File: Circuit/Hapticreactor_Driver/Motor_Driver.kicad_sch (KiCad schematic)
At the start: 5 parts, among them J1 Conn_01x02, J2 Conn_01x02, U2 TB6552FNG_C_8_EL

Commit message: ハプティックリアクタ用基板完成
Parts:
- removed C2: 0.1u, Capacitor_SMD:C_0603_1608Metric_Pad1.08x0.95mm_HandSolder, symbol Device:C
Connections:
- net +5V is gone; now on net +3.3V: U2.6 (VM)
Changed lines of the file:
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@@
 	(paper "A4")
-	(junction
-		(at 199.39 80.01)
-		(diameter 0)
-		(color 0 0 0 0)
-	)
 	(junction
 		(at 172.72 83.82)
@@
 	(wire
 		(pts
-			(xy 199.39 80.01) (xy 207.01 80.01)
-		)
-		(stroke
-			(width 0)
-			(type default)
-		)
-	)
-	(wire
-		(pts
-			(xy 199.39 80.01) (xy 199.39 82.55)
-		)
-		(stroke
-			(width 0)
-			(type default)
-		)
-	)
-	(wire
-		(pts
-			(xy 207.01 76.2) (xy 207.01 80.01)
+			(xy 199.39 76.2) (xy 199.39 82.55)
 		)
 		(stroke
@@
 		(pts
 			(xy 176.53 96.52) (xy 176.53 91.44)
-		)
-		(stroke
-			(width 0)
-			(type default)
-		)
-	)
-	(wire
-		(pts
-			(xy 199.39 76.2) (xy 199.39 80.01)
 		)
 		(stroke
@@
 	)
 	(symbol
-		(lib_id "power:+3.3V")
-		(at 207.01 68.58 0)
-		(unit 1)
-		(exclude_from_sim no)
-		(in_bom yes)
-		(on_board yes)
-		(dnp no)
-		(fields_autoplaced yes)
-		(property "Reference" "#PWR06"
-			(at 207.01 72.39 0)
-			(effects
-				(font
-					(size 1.27 1.27)
-				)
-				(hide yes)
-			)
-		)
-		(property "Value" "+3.3V"
-			(at 207.01 63.5 0)
-			(effects
-				(font
-					(size 1.27 1.27)
-				)
-			)
-		)
-		(property "Footprint" ""
-			(at 207.01 68.58 0)
-			(effects
-				(font
-					(size 1.27 1.27)
-				)
-				(hide yes)
-			)
-		)
-		(property "Datasheet" ""
-			(at 207.01 68.58 0)
-			(effects
-				(font
-					(size 1.27 1.27)
-				)
-				(hide yes)
-			)
-		)
-		(property "Description" "Power symbol creates a global label with name \"+3.3V\""
-			(at 207.01 68.58 0)
-			(effects
-				(font
-					(size 1.27 1.27)
-				)
-				(hide yes)
-			)
-		)
-		(pin "1"
-		)
-		(instances
-			(project "Hapticreactor_Driver"
-				(path "/2de60640-83cc-436b-97a4-426b15b610d6/dde69832-1fdb-4162-bbfc-013df7eb0793"
-					(reference "#PWR06")
-					(unit 1)
-				)
-			)
-		)
-	)
-	(symbol
 		(lib_id "Connector_Generic:Conn_01x02")
 		(at 233.68 80.01 0)
@@
 				(path "/2de60640-83cc-436b-97a4-426b15b610d6/dde69832-1fdb-4162-bbfc-013df7eb0793"
 					(reference "J1")
+					(unit 1)
+				)
+			)
+		)
+	)
+	(symbol
+		(lib_id "power:+3.3V")
+		(at 121.92 69.85 0)
+		(unit 1)
+		(exclude_from_sim no)
+		(in_bom yes)
+		(on_board yes)
+		(dnp no)
+		(fields_autoplaced yes)
+		(property "Reference" "#PWR04"
+			(at 121.92 73.66 0)
+			(effects
+				(font
+					(size 1.27 1.27)
+				)
+				(hide yes)
+			)
+		)
+		(property "Value" "+3.3V"
+			(at 121.92 64.77 0)
+			(effects
+				(font
+					(size 1.27 1.27)
+				)
+			)
+		)
+		(property "Footprint" ""
+			(at 121.92 69.85 0)
+			(effects
+				(font
+					(size 1.27 1.27)
+				)
+				(hide yes)
+			)
+		)
+		(property "Datasheet" ""
+			(at 121.92 69.85 0)
+			(effects
+				(font
+					(size 1.27 1.27)
+				)
+				(hide yes)
+			)
+		)
+		(property "Description" "Power symbol creates a global label with name \"+3.3V\""
+			(at 121.92 69.85 0)
+			(effects
+				(font
+					(size 1.27 1.27)
+				)
+				(hide yes)
+			)
+		)
+		(pin "1"
+		)
+		(instances
+			(project ""
+				(path "/2de60640-83cc-436b-97a4-426b15b610d6/dde69832-1fdb-4162-bbfc-013df7eb0793"
+					(reference "#PWR04")
 					(unit 1)
 				)
@@
 	)
 	(symbol
-		(lib_id "Device:C")
-		(at 207.01 72.39 0)
-		(unit 1)
-		(exclude_from_sim no)
-		(in_bom yes)
-		(on_board yes)
-		(dnp no)
-		(fields_autoplaced yes)
-		(property "Reference" "C2"
-			(at 210.82 71.1199 0)
-			(effects
-				(font
-					(size 1.27 1.27)
-				)
-				(justify left)
-			)
-		)
-		(property "Value" "0.1u"
-			(at 210.82 73.6599 0)
-			(effects
-				(font
-					(size 1.27 1.27)
-				)
-				(justify left)
-			)
-		)
-		(property "Footprint" "Capacitor_SMD:C_0603_1608Metric_Pad1.08x0.95mm_HandSolder"
-			(at 207.9752 76.2 0)
-			(effects
-				(font
-					(size 1.27 1.27)
-				)
-				(hide yes)
-			)
-		)
-		(property "Datasheet" "~"
-			(at 207.01 72.39 0)
-			(effects
-				(font
-					(size 1.27 1.27)
-				)
-				(hide yes)
-			)
-		)
-		(property "Description" "Unpolarized capacitor"
-			(at 207.01 72.39 0)
-			(effects
-				(font
-					(size 1.27 1.27)
-				)
-				(hide yes)
-			)
-		)
-		(pin "1"
-		)
-		(pin "2"
-		)
-		(instances
-			(project "Hapticreactor_Driver"
-				(path "/2de60640-83cc-436b-97a4-426b15b610d6/dde69832-1fdb-4162-bbfc-013df7eb0793"
-					(reference "C2")
-					(unit 1)
-				)
-			)
-		)
-	)
-	(symbol
 		(lib_id "TB6552FNG:TB6552FNG_C_8_EL")
 		(at 127 73.66 0)
@@
 					(unit 1)
 				)
-			)
-		)
-	)
-	(symbol
-		(lib_id "power:+5V")
-		(at 121.92 69.85 0)
-		(unit 1)
-		(exclude_from_sim no)
-		(in_bom yes)
-		(on_board yes)
-		(dnp no)
-		(fields_autoplaced yes)
-		(property "Reference" "#PWR04"
-			(at 121.92 73.66 0)
-			(effects
-				(font
-					(size 1.27 1.27)
-				)
-				(hide yes)
-			)
-		)
-		(property "Value" "+5V"
-			(at 121.92 64.77 0)
-			(effects
-				(font
-					(size 1.27 1.27)
-				)
-			)
-		)
-		(property "Footprint" ""
-			(at 121.92 69.85 0)
-			(effects
-				(font
-					(size 1.27 1.27)
-				)
-				(hide yes)
-			)
-		)
-		(property "Datasheet" ""
-			(at 121.92 69.85 0)
-			(effects
-				(font
-					(size 1.27 1.27)
-				)
-				(hide yes)
-			)
-		)
-		(property "Description" "Power symbol creates a global label with name \"+5V\""
-			(at 121.92 69.85 0)
-			(effects
-				(font
-					(size 1.27 1.27)
-				)
-				(hide yes)
-			)
-		)
-		(pin "1"
-		)
-		(instances
-			(project ""
-				(path "/2de60640-83cc-436b-97a4-426b15b610d6/dde69832-1fdb-4162-bbfc-013df7eb0793"
-					(reference "#PWR04")
-					(unit 1)
-				)

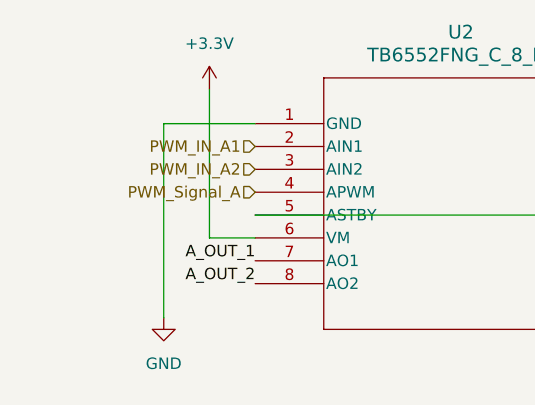
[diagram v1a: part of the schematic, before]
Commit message: VMをバッテリ入力に変更，バッテリ周りの間違いを訂正
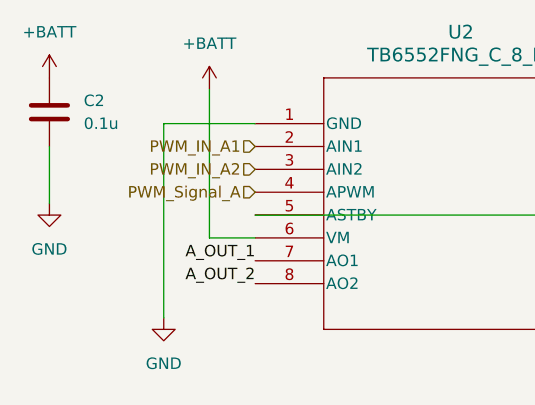
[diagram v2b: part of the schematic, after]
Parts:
- added C2: 0.1u, Capacitor_SMD:C_0603_1608Metric_Pad1.08x0.95mm_HandSolder, symbol Device:C
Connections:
- net +3.3V: no longer U2.6 (VM)
- net GND: now also C2.2
- new net +BATT: C2.1, U2.6 (VM)

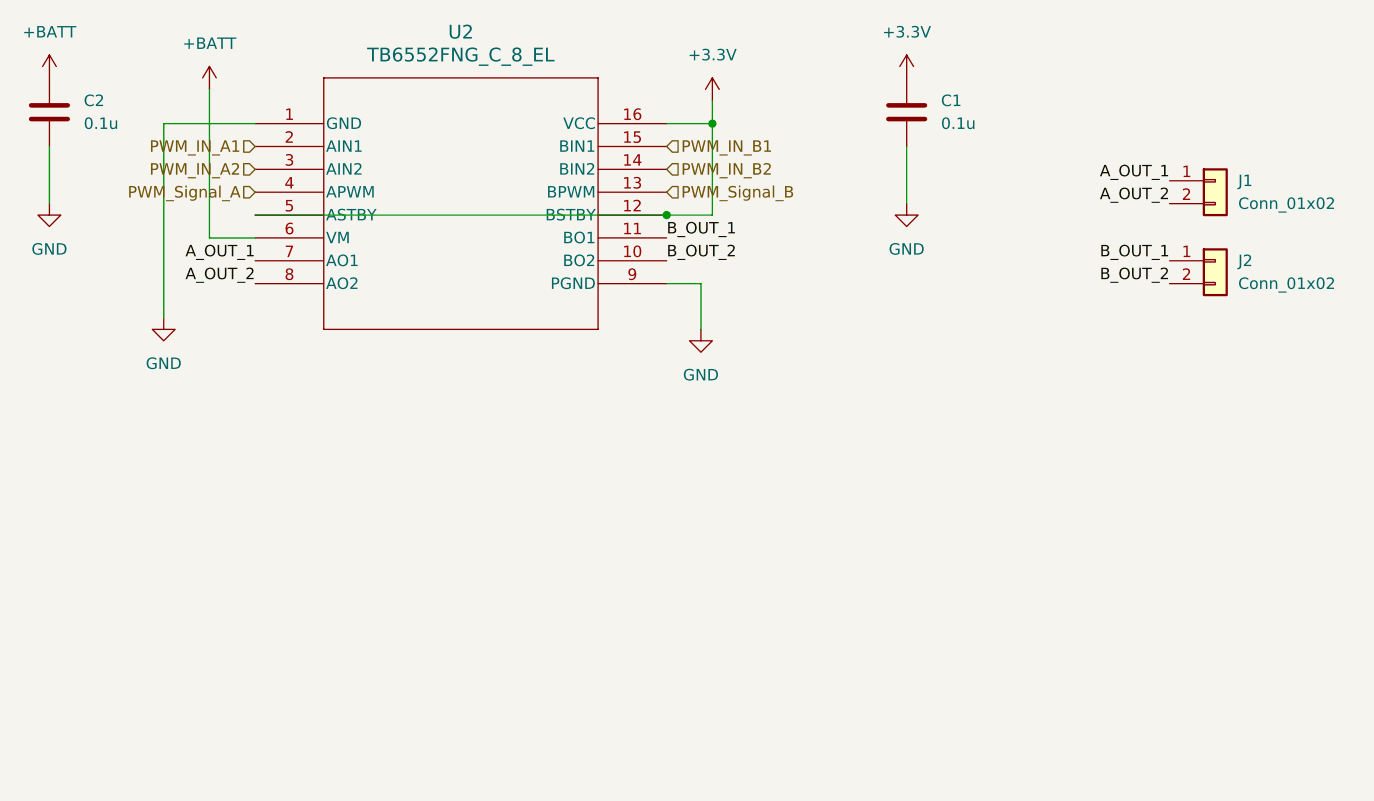
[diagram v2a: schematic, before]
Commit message: 秋野の回路に昇圧DCDCつけて東芝MDつけた
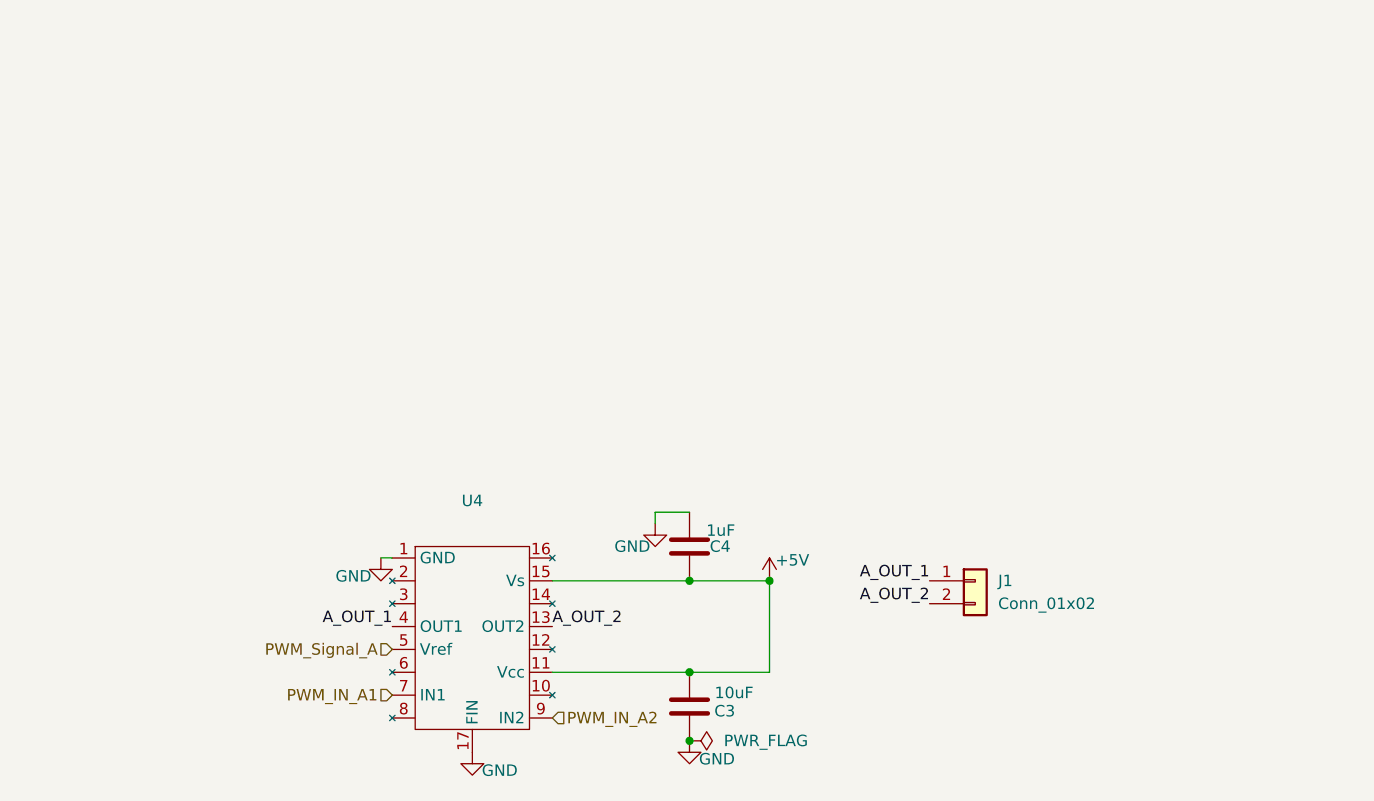
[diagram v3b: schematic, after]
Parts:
- removed C1, C2: 0.1u, Capacitor_SMD:C_0603_1608Metric_Pad1.08x0.95mm_HandSolder, symbol Device:C
- removed J2: Conn_01x02, Connector_PinHeader_2.00mm:PinHeader_1x02_P2.00mm_Vertical, symbol Connector_Generic:Conn_01x02
- removed U2: TB6552FNG_C_8_EL, User:TB6552FNG, symbol TB6552FNG:TB6552FNG_C_8_EL
- added C3: 10uF, Capacitor_SMD:C_0603_1608Metric, symbol Device:C
- added C4: 1uF, Capacitor_SMD:C_0603_1608Metric, symbol Device:C
- added U4: ~, 0_MyFootprintLibrary:TA7291F, symbol 0_MySymbolLibrary:TA7291F
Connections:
- net A_OUT_1: now also U4.4 (OUT1)
- net A_OUT_2: now also U4.13 (OUT2)
- net GND: now also C3.1, C4.2, U4.1 (GND), U4.17 (FIN)
- net PWM_IN_A1: now also U4.7 (IN1)
- net PWM_IN_A2: now also U4.9 (IN2)
- net PWM_Signal_A: now also U4.5 (Vref)
- new net +5V: C3.2, C4.1, U4.11 (Vcc), U4.15 (Vs)
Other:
- moved on the sheet: J1
